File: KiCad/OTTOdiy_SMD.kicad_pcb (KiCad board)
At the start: 4 copper layers, 297 x 170.8 mm, 468 parts, among them CN201 1x4 MALE 1.5mm, CN202 1x4 MALE 1.5mm, J201 RASPBERRY PI 3 A+, J202 Conn_02x03, J203 Conn_02x05, J204 Conn_02x05, J205 Conn_02x04, J206 Conn_02x06, J207 Conn_02x03, Q201 IRF9321PbF, SW1 ALPS SKHC, SW10 ALPS SKHC, SW11 ALPS SKHC, SW12 ALPS SKHC, SW13 ALPS SKHC, SW14 ALPS SKHC, SW15 ALPS SKHC, SW16 ALPS SKHC, SW17 ALPS SKHC, SW18 ALPS SKHC, SW19 ALPS SKHC, SW2 ALPS SKHC, SW20 ALPS SKHC, SW201 SW_Push, SW202 SW_DIP_x02, SW203 ALPS SKHH angled, SW21 ALPS SKHC, SW22 ALPS SKHC, SW23 ALPS SKHC, SW24 ALPS SKHC, SW25 ALPS SKHC, SW26 ALPS SKHC, SW27 6x6x13mm, SW28 6x6x13mm, SW29 6x6x13mm, SW3 ALPS SKHC, SW30 6x6x13mm, SW31 6x6x13mm, SW32 6x6x13mm, SW33 6x6x13mm, SW34 6x6x13mm, SW35 6x6x13mm, SW36 6x6x13mm, SW37 6x6x13mm, SW38 6x6x13mm, SW39 6x6x13mm, SW4 ALPS SKHC, SW40 6x6x13mm, SW41 6x6x13mm, SW42 6x6x13mm, SW43 6x6x13mm, SW44 6x6x13mm, SW45 6x6x13mm, SW46 6x6x13mm, SW47 6x6x13mm, SW5 ALPS SKHC, SW6 ALPS SKHC, SW7 ALPS SKHC, SW8 ALPS SKHC, SW9 ALPS SKHC, U201 TPS79533, U202 STM32F407VGTx, U203 74HC125D, U204 USB6B1, U205 74HC14, U206 H11L1, U207 WM8731-Audio, U208 TPS79533, Y201 8MHz, Y202 32.768kHz, Y203 12.288MHz

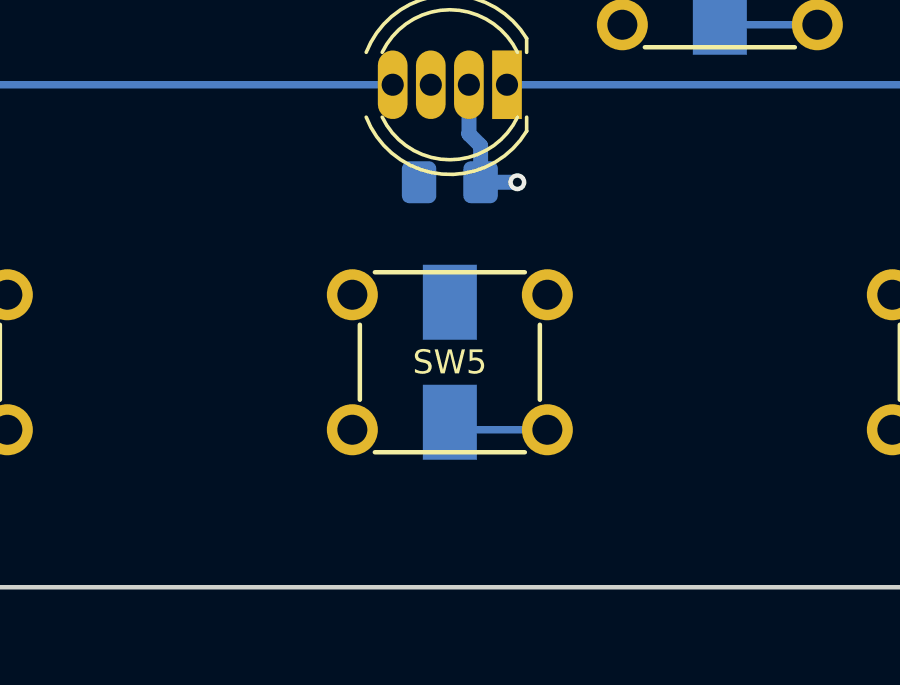
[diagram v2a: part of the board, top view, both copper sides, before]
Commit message: add switch and encoder parts. BM Complete. Footprints complete.
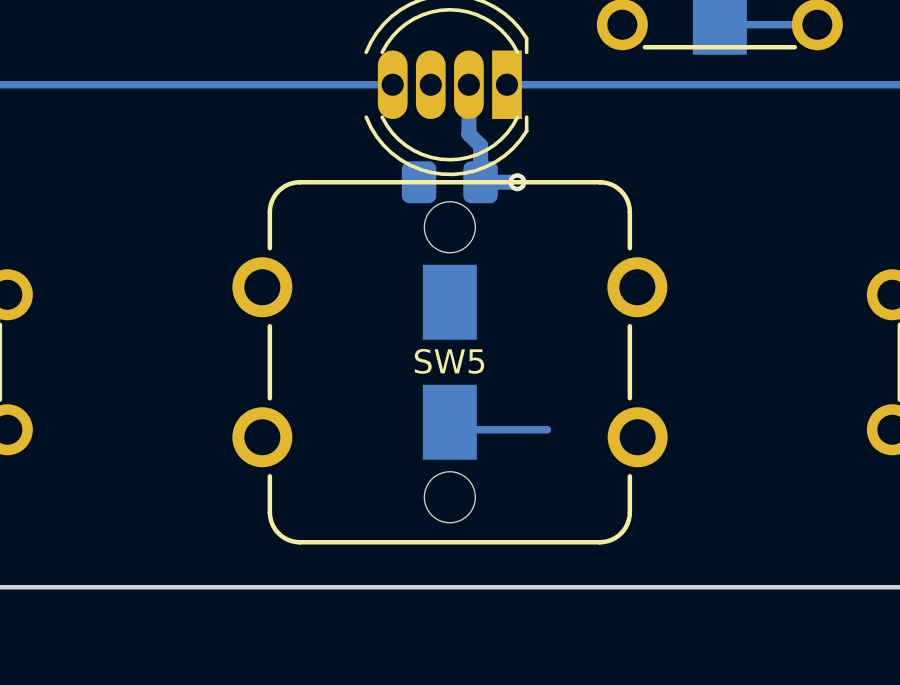
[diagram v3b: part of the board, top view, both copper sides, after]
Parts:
- SW5: footprint Spatz:6x6mm_Switch_LargeCap -> OTTO_Footprints_Lib:ALPS_SKHC

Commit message: Add power switch and other misc nice to haves
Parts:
- removed C201, C208, C209: 10µF, Capacitor_SMD:C_0805_2012Metric_Pad1.15x1.40mm_HandSolder
- removed C202: 1nF/2kV, Capacitor_SMD:C_1206_3216Metric_Pad1.42x1.75mm_HandSolder
- removed C206, C207: 12.5pF, Capacitor_SMD:C_0805_2012Metric_Pad1.15x1.40mm_HandSolder
- removed C228, C229: 1000µF, Capacitor_THT:CP_Radial_D8.0mm_P3.50mm
- removed D201: 5.6V, Diode_SMD:D_SMA
- removed DUMMY201: RASPBERRY PI 3 A+, Spatz:Raspberry Pi A
- removed DUMMY202: FE-PI AUDIO Z V2, Spatz:Raspberry Pi Zero - (minus 1 hole)
- removed F201: 3A, Fuse:Fuse_1806_4516Metric_Pad1.57x1.80mm_HandSolder
- removed the H205 at (306.2, 89.8)
- removed the H205 at (306.2, 31.8)
- removed JP201: SolderJumper_3_Open, Jumper:SolderJumper-3_P2.0mm_Open_TrianglePad1.0x1.5mm
- removed Q201: IRF9321PbF, Package_SO:SOIC-8_3.9x4.9mm_P1.27mm
- removed R201: 1M, Resistor_SMD:R_1206_3216Metric_Pad1.42x1.75mm_HandSolder
- removed R209: 10k, Resistor_SMD:R_0805_2012Metric_Pad1.15x1.40mm_HandSolder
- removed R210: 100k, Resistor_SMD:R_0805_2012Metric_Pad1.15x1.40mm_HandSolder
- removed REF**: PinSocket_2x20_P2.54mm_Vertical_SMD, Connector_PinSocket_2.54mm:PinSocket_2x20_P2.54mm_Vertical_SMD
- removed REF** (x25): SOD-123, digikey-footprints:SOD-123
- removed REF** (x25): LED_WS2812B_PLCC4_5.0x5.0mm_P3.2mm, LED_SMD:LED_WS2812B_PLCC4_5.0x5.0mm_P3.2mm
- removed REF** (x25): SW_SPST_B3S-1000, Button_Switch_SMD:SW_SPST_B3S-1000
- removed REF** (x25): C_0805_2012Metric, Capacitor_SMD:C_0805_2012Metric
- removed REF** (x5): PJ-393-7A, Connector_Audio:PJ-393-7A
- removed REF**: Display_2.8inch_IPS3P4416-H-E, OTTOdiy - SMD - Production:Display_2.8inch_IPS3P4416-H-E
- removed REF** (x4): ALPS_EC12D, Rotary_Encoder:ALPS_EC12D
- removed U201: TPS79533, Package_TO_SOT_SMD:SOT-223-6
- removed U203: 74HC125D, Package_SO:SOIC-14_3.9x8.7mm_P1.27mm
- added C77: 10nF, Capacitor_SMD:C_0805_2012Metric_Pad1.15x1.40mm_HandSolder, F.Cu at (206.8, 54.0)
- added C78: 100nF, Capacitor_SMD:C_0805_2012Metric_Pad1.15x1.40mm_HandSolder, F.Cu at (221.9, 56.9)
- added C79: 470uF, Capacitor_SMD:C_Elec_6.3x7.7, F.Cu at (181.6, 44.6)
- added C80: 10uF, Capacitor_SMD:C_0805_2012Metric_Pad1.15x1.40mm_HandSolder, F.Cu at (198.4, 59.9)
- added C81: 470uF, Capacitor_SMD:C_Elec_6.3x7.7, F.Cu at (192.1, 39.2)
- added C82: 100nF, Capacitor_SMD:C_0805_2012Metric_Pad1.15x1.40mm_HandSolder, F.Cu at (193.6, 63.2)
- added C83: 100nF, Capacitor_SMD:C_0805_2012Metric_Pad1.15x1.40mm_HandSolder, F.Cu at (202.1, 54.0)
- added C84: 470uF, Capacitor_SMD:C_Elec_6.3x7.7, F.Cu at (168.6, 54.9)
- added C85: 1uF, Capacitor_SMD:C_0805_2012Metric_Pad1.15x1.40mm_HandSolder, F.Cu at (203.1, 59.9)
- added C86: 4.7uF, Capacitor_SMD:C_0805_2012Metric_Pad1.15x1.40mm_HandSolder, F.Cu at (203.1, 57.0)
- added C87: 10nF, Capacitor_SMD:C_0805_2012Metric_Pad1.15x1.40mm_HandSolder, F.Cu at (212.7, 45.5)
- added C88: 10uF, Capacitor_SMD:C_0805_2012Metric_Pad1.15x1.40mm_HandSolder, F.Cu at (211.7, 48.4)
- added C89: 22pF, Capacitor_SMD:C_0805_2012Metric_Pad1.15x1.40mm_HandSolder, F.Cu at (198.4, 62.9)
- added C90: 100nF, Capacitor_SMD:C_0805_2012Metric_Pad1.15x1.40mm_HandSolder, F.Cu at (207.0, 50.4)
- added C91: 100nF, Capacitor_SMD:C_0805_2012Metric_Pad1.15x1.40mm_HandSolder, F.Cu at (212.7, 42.5)
- added C92: 680pF, Capacitor_SMD:C_0805_2012Metric_Pad1.15x1.40mm_HandSolder, F.Cu at (202.2, 51.1)
- added C93: 15pF, Capacitor_SMD:C_0805_2012Metric_Pad1.15x1.40mm_HandSolder, F.Cu at (193.6, 60.2)
- added C94: 47pF, Capacitor_SMD:C_0805_2012Metric_Pad1.15x1.40mm_HandSolder, F.Cu at (193.6, 57.3)
- added C95: 47uF, Capacitor_SMD:C_1206_3216Metric_Pad1.42x1.75mm_HandSolder, F.Cu at (172.5, 61.2)
- added C96: 15pF, Capacitor_SMD:C_0805_2012Metric_Pad1.15x1.40mm_HandSolder, F.Cu at (173.5, 72.3)
- added C97: 15pF, Capacitor_SMD:C_0805_2012Metric_Pad1.15x1.40mm_HandSolder, F.Cu at (170.7, 78.1)
- added D48: 15V BI TVS, Diode_SMD:D_SOD-123F, F.Cu at (178.3, 61.2)
- added D49: 15V ZENER, Diode_SMD:D_SOD-123, F.Cu at (198.0, 45.0)
- added D50: 6V BI TVS, Package_TO_SOT_SMD:SOT-323_SC-70_Handsoldering, F.Cu at (192.9, 69.7)
- added D51: 6V BI TVS, Package_TO_SOT_SMD:SOT-323_SC-70_Handsoldering, F.Cu at (192.9, 73.4)
- added D52: 6V BI TVS, Package_TO_SOT_SMD:SOT-323_SC-70_Handsoldering, F.Cu at (198.8, 69.7)
- added D53: 6V BI TVS, Package_TO_SOT_SMD:SOT-323_SC-70_Handsoldering, F.Cu at (192.9, 77.0)
- added D54: 6V BI TVS, Package_TO_SOT_SMD:SOT-323_SC-70_Handsoldering, F.Cu at (198.8, 73.4)
- added D55: 6V BI TVS, Package_TO_SOT_SMD:SOT-323_SC-70_Handsoldering, F.Cu at (204.6, 69.7)
- added D56: 6V BI TVS, Package_TO_SOT_SMD:SOT-323_SC-70_Handsoldering, F.Cu at (198.8, 77.0)
- added FB1: 1kΩ@100Mhz, Inductor_SMD:L_0805_2012Metric_Pad1.15x1.40mm_HandSolder, F.Cu at (175.5, 75.3)
- added J1: Conn_ARM_JTAG_SWD_10, OTTO_Footprints_Lib:FTSH-105-01-X-DV-K, F.Cu at (167.3, 72.3)
- added J2: JST 2-pin SH, Connector_JST:JST_SH_SM02B-SRSS-TB_1x02-1MP_P1.00mm_Horizontal, F.Cu at (115.8, 54.6)
- added J3: JST 2-pin SH, Connector_JST:JST_SH_SM02B-SRSS-TB_1x02-1MP_P1.00mm_Horizontal, F.Cu at (122.7, 54.6)
- added L1: 4.7uH, OTTO_Footprints_Lib:L_7.3x6.6_H3, F.Cu at (201.3, 39.1)
- added L2: 2.2uH, OTTO_Footprints_Lib:L_7.3x6.6_H3, F.Cu at (190.8, 47.2)
- added Q1: AO4485, Package_SO:SOIC-8_3.9x4.9mm_P1.27mm, F.Cu at (185.9, 54.4)
- added R1: 1k, Resistor_SMD:R_0805_2012Metric_Pad1.15x1.40mm_HandSolder, F.Cu at (226.6, 36.6)
- added R10: 100k, Resistor_SMD:R_0805_2012Metric_Pad1.15x1.40mm_HandSolder, F.Cu at (198.4, 57.0)
- added R11: 100k, Resistor_SMD:R_0805_2012Metric_Pad1.15x1.40mm_HandSolder, F.Cu at (227.7, 52.2)
- added R12: 0, Resistor_SMD:R_0805_2012Metric_Pad1.15x1.40mm_HandSolder, F.Cu at (207.0, 47.4)
- added R13: 100k, Resistor_SMD:R_0805_2012Metric_Pad1.15x1.40mm_HandSolder, F.Cu at (188.9, 62.0)
- added R14: 100k, Resistor_SMD:R_0805_2012Metric_Pad1.15x1.40mm_HandSolder, F.Cu at (208.0, 44.2)
- added R15: 100k, Resistor_SMD:R_0805_2012Metric_Pad1.15x1.40mm_HandSolder, F.Cu at (197.5, 48.1)
- added R16: 100k, Resistor_SMD:R_0805_2012Metric_Pad1.15x1.40mm_HandSolder, F.Cu at (203.2, 44.5)
- added R17: 0, Resistor_SMD:R_0805_2012Metric_Pad1.15x1.40mm_HandSolder, F.Cu at (188.9, 59.1)
- added R18: 182k, Resistor_SMD:R_0805_2012Metric_Pad1.15x1.40mm_HandSolder, F.Cu at (208.0, 41.3)
- added R19: 40.2k, Resistor_SMD:R_0805_2012Metric_Pad1.15x1.40mm_HandSolder, F.Cu at (197.5, 51.1)
- added R2: 1k, Resistor_SMD:R_0805_2012Metric_Pad1.15x1.40mm_HandSolder, F.Cu at (221.9, 36.6)
- added R20: 42.2k, Resistor_SMD:R_0805_2012Metric_Pad1.15x1.40mm_HandSolder, F.Cu at (212.8, 36.6)
- added R21: 33k, Resistor_SMD:R_0805_2012Metric_Pad1.15x1.40mm_HandSolder, F.Cu at (202.2, 48.1)
- added R22: 845k, Resistor_SMD:R_0805_2012Metric_Pad1.15x1.40mm_HandSolder, F.Cu at (211.7, 51.4)
- added R23: 158k, Resistor_SMD:R_0805_2012Metric_Pad1.15x1.40mm_HandSolder, F.Cu at (212.8, 39.6)
- added R235: 33, Resistor_SMD:R_0805_2012Metric_Pad1.15x1.40mm_HandSolder, F.Cu at (208.8, 73.0)
- added R236: 33, Resistor_SMD:R_0805_2012Metric_Pad1.15x1.40mm_HandSolder, F.Cu at (204.1, 76.0)
- added R237: 33, Resistor_SMD:R_0805_2012Metric_Pad1.15x1.40mm_HandSolder, F.Cu at (209.9, 69.4)
- added R238: 33, Resistor_SMD:R_0805_2012Metric_Pad1.15x1.40mm_HandSolder, F.Cu at (204.1, 73.0)
- added R24: 10k, Resistor_SMD:R_0805_2012Metric_Pad1.15x1.40mm_HandSolder, F.Cu at (197.3, 54.0)
- added R3: 1k, Resistor_SMD:R_0805_2012Metric_Pad1.15x1.40mm_HandSolder, F.Cu at (221.9, 39.6)
- added R4: 10k, Resistor_SMD:R_0805_2012Metric_Pad1.15x1.40mm_HandSolder, F.Cu at (183.0, 72.3)
- added R5: 10k, Resistor_SMD:R_0805_2012Metric_Pad1.15x1.40mm_HandSolder, F.Cu at (183.0, 69.4)
- added R6: 10k, Resistor_SMD:R_0805_2012Metric_Pad1.15x1.40mm_HandSolder, F.Cu at (178.2, 72.3)
- added R7: 10k, Resistor_SMD:R_0805_2012Metric_Pad1.15x1.40mm_HandSolder, F.Cu at (178.2, 69.4)
- added R8: 40.2k, Resistor_SMD:R_0805_2012Metric_Pad1.15x1.40mm_HandSolder, F.Cu at (173.5, 69.4)
- added R9: 100k, Resistor_SMD:R_0805_2012Metric_Pad1.15x1.40mm_HandSolder, F.Cu at (226.6, 56.9)
- added SW48: SW_DIP_x02, OTTO_Footprints_Lib:SW_DIP_SPSTx02_Slide_HRO_EP-02KS, F.Cu at (181.9, 37.8)
- added SW49: SW_SPDT, Button_Switch_SMD:SW_SPDT_CK-JS102011SAQN, F.Cu at (79.0, 107.7)
- added TP1: TestPoint, TestPoint:TestPoint_Keystone_5000-5004_Miniature, F.Cu at (232.2, 52.9)
- added TP10: TestPoint, TestPoint:TestPoint_Keystone_5000-5004_Miniature, F.Cu at (180.0, 76.0)
- added TP11: TestPoint, TestPoint:TestPoint_Keystone_5000-5004_Miniature, F.Cu at (114.6, 60.6)
- added TP12: TestPoint, TestPoint:TestPoint_Keystone_5000-5004_Miniature, F.Cu at (118.9, 60.6)
- added TP13: TestPoint, TestPoint:TestPoint_Keystone_5000-5004_Miniature, F.Cu at (128.3, 53.0)
- added TP14: TestPoint, TestPoint:TestPoint_Keystone_5000-5004_Miniature, F.Cu at (123.3, 60.6)
- added TP15: TestPoint, TestPoint:TestPoint_Keystone_5000-5004_Miniature, F.Cu at (128.3, 57.3)
- added TP2: TestPoint, TestPoint:TestPoint_Keystone_5000-5004_Miniature, F.Cu at (239.5, 41.7)
- added TP3: TestPoint, TestPoint:TestPoint_Keystone_5000-5004_Miniature, F.Cu at (235.1, 41.7)
- added TP4: TestPoint, TestPoint:TestPoint_Keystone_5000-5004_Miniature, F.Cu at (235.5, 37.3)
- added TP5: TestPoint, TestPoint:TestPoint_Keystone_5000-5004_Miniature, F.Cu at (230.8, 41.7)
- added TP6: TestPoint, TestPoint:TestPoint_Keystone_5000-5004_Miniature, F.Cu at (226.0, 44.6)
- added TP7: TestPoint, TestPoint:TestPoint_Keystone_5000-5004_Miniature, F.Cu at (231.2, 37.3)
- added TP8: TestPoint, TestPoint:TestPoint_Keystone_5000-5004_Miniature, F.Cu at (226.4, 40.3)
- added TP9: TestPoint, TestPoint:TestPoint_Keystone_5000-5004_Miniature, F.Cu at (221.7, 43.2)
- added U1: SN74LV1T125_SOT-23_A, Package_TO_SOT_SMD:SOT-23-5_HandSoldering, F.Cu at (222.4, 53.1)
- added U2: TPS22918_SOT23-6_A, Package_TO_SOT_SMD:SOT-23-6, F.Cu at (208.0, 37.5)
- added U3: LTC3112_TSSOP20_A, OTTO_Footprints_Lib:TSSOP-20_FE_CA, F.Cu at (177.6, 55.6)
- added U4: TLV62568_SOT-23-5_A, Package_TO_SOT_SMD:SOT-23-5, F.Cu at (192.5, 53.5)
- added U5: TPS22918_SOT23-6_A, Package_TO_SOT_SMD:SOT-23-6, F.Cu at (184.1, 59.9)
- BT201: value CR1220 -> CR1220 HOLDER; footprint Battery:QJ1220-2SMT -> OTTO_Footprints_Lib:QJ1220-2SMT
- C1, C10, C11, C12, C13, C14, C15, C16, C17, C18, C19, C2, C20, C21, C22, C23, C24, C25, C26, C27, C28, C29, C3, C30, C31, C32, C33, C34, C35, C36, C37, C38, C39, C4, C40, C41, C42, C43, C44, C45, C46, C47, C48, C49, C5, C50, C51, C52, C53, C54, C55, C56, C58, C59, C6, C60, C61, C62, C63, C64, C65, C66, C67, C68, C69, C7, C70, C71, C72, C73, C74, C75, C8, C9: footprint Capacitor_SMD:C_0805_2012Metric_Pad1.15x1.40mm_HandSolder_marked -> Capacitor_SMD:C_0805_2012Metric_Pad1.15x1.40mm_HandSolder
- C204, C205: value 20pF -> 30pF
- C211: value 4.7µF -> 4.7uF
- C218, C219, C223: value 1µF -> 1uF
- C221, C222: value 2.2µF -> 2.2uF
- C226, C232, C260, C261, C267, C268: value 10µF -> 10uF
- C243, C246, C247, C250, C264: value 10µ -> 10uF
- C251, C253, C254, C255, C257: value 1µF (AUDIO) -> 1uF (AUDIO); footprint Capacitor_THT:C_Rect_L7.2mm_W5.0mm_P5.00mm_FKS2_FKP2_MKS2_MKP2 -> OTTO_Footprints_Lib:C_Rect_L7.2mm_W5.0mm_P5.00mm_FKS2_FKP2_MKS2_MKP2
- C252, C256, C259: value 220p (C0G) -> 220pF (C0G)
- C258, C262: value 220µF -> 220uF
- C265, C266: value 20pF -> 30pF; moved to F.Cu
- C57: footprint Capacitor_SMD:C_0805_2012Metric_Pad1.15x1.40mm_HandSolder_marked -> Capacitor_SMD:C_0805_2012Metric_Pad1.15x1.40mm_HandSolder; moved to F.Cu
- C76: value 100nF -> 47uF; footprint Capacitor_SMD:C_0805_2012Metric_Pad1.15x1.40mm_HandSolder_marked -> Capacitor_SMD:C_1206_3216Metric_Pad1.42x1.75mm_HandSolder; moved to F.Cu
- CN201, CN202: value 1x4 MALE 1.5mm -> 1x4 MALE Molex PicoBlade; footprint Connector_Molex:Molex_PicoBlade_53048-0410_1x04_P1.25mm_Horizontal -> Connector_Molex:Molex_PicoBlade_53261-0471_1x04-1MP_P1.25mm_Horizontal
- D1, D10, D11, D12, D13, D14, D15, D16, D17, D18, D19, D2, D20, D202, D203, D204, D205, D21, D22, D23, D24, D25, D26, D27, D28, D29, D3, D30, D31, D32, D33, D34, D35, D36, D37, D38, D39, D4, D40, D41, D42, D43, D44, D45, D46, D47, D5, D6, D7, D8, D9: value M7 -> SM4007PL; footprint Diode_SMD:D_SMA -> Diode_SMD:D_SOD-123F
- D206: value 1N4148 -> 1N4148W; footprint Diode_SMD:D_SMA -> Diode_SMD:D_SOD-123
- DC201: value Barrel_Jack_Switch -> Barrel Jack, 2.0mmID, 6.5mmOD; footprint Spatz:DC Jack -> OTTO_Footprints_Lib:BarrelJack_2.0mmID_6.5mmOD
- DISPLAY201: value 2.8INCH_IPS_SPI -> 2.8 Inch IPS Display, SPI Interface; footprint Spatz:2.8 INCH IPS DISPLAY -> OTTO_Footprints_Lib:2.8_INCH_IPS_DISPLAY
- ENC1, ENC2, ENC3, ENC4: footprint Spatz:ALPS EC11 -> OTTO_Footprints_Lib:ALPS_EC11
- H201, H202, H203, H204, H205, H206, H207, H208, H209, H210, H211: footprint Spatz:Mounting_Hole_M2.5_Loose_Fit -> OTTO_Footprints_Lib:Mounting_Hole_M2.5_Loose_Fit
- J201: value RASPBERRY PI 3 A+ -> Raspberry Pi Connector; footprint Connector_Harwin:Harwin_M20-7812045_2x20_P2.54mm_Vertical_SolderHoles -> OTTO_Footprints_Lib:Raspberry_Pi_A_FacingDown_TH
- J206: footprint Connector_Harwin:Harwin_M20-7810645_2x06_P2.54mm_Vertical_SolderHoles -> OTTO_Footprints_Lib:Harwin_M20-7810645_2x06_P2.54mm_Vertical_SolderHoles
- J207: footprint Connector_Harwin:Harwin_M20-7810345_2x03_P2.54mm_Vertical_SolderHoles -> OTTO_Footprints_Lib:Harwin_M20-7810345_2x03_P2.54mm_Vertical_SolderHoles
- LED1, LED10, LED11, LED12, LED13, LED14, LED15, LED16, LED17, LED18, LED19, LED2, LED20, LED21, LED22, LED23, LED24, LED25, LED26, LED27, LED28, LED29, LED3, LED30, LED31, LED32, LED33, LED34, LED35, LED36, LED37, LED38, LED39, LED4, LED40, LED41, LED42, LED43, LED44, LED45, LED46, LED47, LED5, LED6, LED7, LED8, LED9: value WS2812D-F5 -> WS2812D-5; footprint Spatz:LED_D5.0mm-4 -> OTTO_Footprints_Lib:LED_D5.0mm-4
- MK201: footprint Sensor_Audio:INGHAi GMI6050p -> OTTO_Footprints_Lib:INGHAi_GMI6050p
- PHOTO201: footprint OptoDevice:ALS-PDIC243-3B -> OTTO_Footprints_Lib:ALS-PDIC243-3B
- R202, R205, R206, R207: value 2k2 -> 2.2k
- R208: value 470 -> 100
- SW1, SW10, SW11, SW12, SW13, SW14, SW15, SW16, SW17, SW18, SW19, SW2, SW20, SW21, SW22, SW23, SW24, SW25, SW26, SW3, SW4, SW6, SW7, SW8, SW9: value ALPS SKHC -> ALPS SKHH OR SKPF; footprint Spatz:6x6mm_Switch_LargeCap -> OTTO_Footprints_Lib:6x6mm_Switch_LargeCap_ALT_SKPF
- SW201: value SW_Push -> 6x6x5mm
- SW202: footprint Button_Switch_THT:XKB_DSIC02LH-P -> OTTO_Footprints_Lib:SW_DIP_SPSTx02_Slide_HRO_EP-02KS
- SW203: value ALPS SKHH angled -> 6x6x5.85mm (RA)
- SW27, SW28, SW29, SW30, SW31, SW32, SW33, SW34, SW35, SW36, SW37, SW38, SW39, SW40, SW41, SW42, SW43, SW44, SW45, SW46, SW47: footprint Spatz:6x6mm_Switch -> OTTO_Footprints_Lib:6x6mm_Switch
- SW5: value ALPS SKHC -> ALPS SKHH OR SKPF; footprint OTTO_Footprints_Lib:ALPS_SKHC -> OTTO_Footprints_Lib:6x6mm_Switch_LargeCap_ALT_SKPF
- TRS201, TRS202, TRS203: value PJ-393-7A -> PJ-3930-8A; footprint Spatz:3.5mm_jack_PJ-3930-8A -> OTTO_Footprints_Lib:3.5mm_jack_PJ-3930-8A
- TRS204, TRS205, TRS206: footprint Spatz:3.5mm_jack_PJ-3930-8A -> OTTO_Footprints_Lib:3.5mm_jack_PJ-3930-8A
- U205: value 74HC14 -> SN74HC14
- U206: value H11L1 -> H11L1S; footprint Package_DIP:DIP-6_W7.62mm_SMDSocket_SmallPads -> Package_DIP:SMDIP-6_W7.62mm
- U207: value WM8731-Audio -> WM8731
- USB201: footprint Spatz:USB_B -> OTTO_Footprints_Lib:USB_B
- Y201, Y203: footprint Crystal:Crystal_HC49-U_Vertical -> Crystal:Crystal_SMD_HC49-SD_HandSoldering
- Y202: footprint Crystal:Crystal_DS26_D2.0mm_L6.0mm_Horizontal -> Crystal:Crystal_SMD_SeikoEpson_MC306-4Pin_8.0x3.2mm_HandSoldering
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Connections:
- net +5V_IN renamed +5V_REG
- net /AUDIO/XTI renamed Net-(C265-Pad1)
- net /AUDIO/XTO renamed Net-(C266-Pad1)
- C1 pad 1: +5V_MAIN -> +5V_LEDS
- C10 pad 1: +5V_MAIN -> +5V_LEDS
- C11 pad 1: +5V_MAIN -> +5V_LEDS
- C12 pad 1: +5V_MAIN -> +5V_LEDS
- C13 pad 1: +5V_MAIN -> +5V_LEDS
- C14 pad 1: +5V_MAIN -> +5V_LEDS
- C15 pad 1: +5V_MAIN -> +5V_LEDS
- C16 pad 1: +5V_MAIN -> +5V_LEDS
- C17 pad 1: +5V_MAIN -> +5V_LEDS
- C18 pad 1: +5V_MAIN -> +5V_LEDS
- C19 pad 1: +5V_MAIN -> +5V_LEDS
- C2 pad 1: +5V_MAIN -> +5V_LEDS
- C20 pad 1: +5V_MAIN -> +5V_LEDS
- C21 pad 1: +5V_MAIN -> +5V_LEDS
- C219 pad 1: +3V3_MCU -> +3V3A_MCU
- C22 pad 1: +5V_MAIN -> +5V_LEDS
- C223 pad 1: Net-(C223-Pad1) -> +3V3A_MCU
- C23 pad 1: +5V_MAIN -> +5V_LEDS
- C24 pad 1: +5V_MAIN -> +5V_LEDS
- C25 pad 1: +5V_MAIN -> +5V_LEDS
- C26 pad 1: +5V_MAIN -> +5V_LEDS
- C261 pad 2: +5V_MAIN -> +5V_PI
- C267 pad 2: +5V_MAIN -> +5V_PI
- C27 pad 1: +5V_MAIN -> +5V_LEDS
- C28 pad 1: +5V_MAIN -> +5V_LEDS
- C29 pad 1: +5V_MAIN -> +5V_LEDS
- C3 pad 1: +5V_MAIN -> +5V_LEDS
- C30 pad 1: +5V_MAIN -> +5V_LEDS
- C31 pad 1: +5V_MAIN -> +5V_LEDS
- C32 pad 1: +5V_MAIN -> +5V_LEDS
- C33 pad 1: +5V_MAIN -> +5V_LEDS
- C34 pad 1: +5V_MAIN -> +5V_LEDS
- C35 pad 1: +5V_MAIN -> +5V_LEDS
- C36 pad 1: +5V_MAIN -> +5V_LEDS
- C37 pad 1: +5V_MAIN -> +5V_LEDS
- C38 pad 1: +5V_MAIN -> +5V_LEDS
- C39 pad 1: +5V_MAIN -> +5V_LEDS
- C4 pad 1: +5V_MAIN -> +5V_LEDS
- C40 pad 1: +5V_MAIN -> +5V_LEDS
- C41 pad 1: +5V_MAIN -> +5V_LEDS
- C42 pad 1: +5V_MAIN -> +5V_LEDS
- C43 pad 1: +5V_MAIN -> +5V_LEDS
- C44 pad 1: +5V_MAIN -> +5V_LEDS
- C45 pad 1: +5V_MAIN -> +5V_LEDS
- C46 pad 1: +5V_MAIN -> +5V_LEDS
- C47 pad 1: +5V_MAIN -> +5V_LEDS
- C48 pad 2: ICP_RST -> /ICP_RST
- C5 pad 1: +5V_MAIN -> +5V_LEDS
- C55 pad 1: +3V3_MCU -> +3V3A_MCU
- C56 pad 1: Net-(C223-Pad1) -> +3V3A_MCU
- C57 pad 1: +5V_MCU -> GND
- C57 pad 2: GND -> Net-(C57-Pad2)
- C6 pad 1: +5V_MAIN -> +5V_LEDS
- C7 pad 1: +5V_MAIN -> +5V_LEDS
- C76 pad 1: Net-(C76-Pad1) -> /MCU/PERIPHERALS/+5V_REG
- C8 pad 1: +5V_MAIN -> +5V_LEDS
- C9 pad 1: +5V_MAIN -> +5V_LEDS
- CN201 pad 1: Net-(CN201-Pad1) -> (no net)
- CN202 pad 3: Net-(CN202-Pad3) -> (no net)
- D1 pad 1: Net-(D1-Pad1) -> /MCU/ROW_4
- D10 pad 1: Net-(D10-Pad1) -> /MCU/ROW_6
- D11 pad 1: Net-(D11-Pad1) -> /MCU/ROW_8
- D12 pad 1: Net-(D12-Pad1) -> /MCU/ROW_2
- D13 pad 1: Net-(D13-Pad1) -> /MCU/ROW_3
- D14 pad 1: Net-(D14-Pad1) -> /MCU/ROW_5
- D15 pad 1: Net-(D15-Pad1) -> /MCU/ROW_6
- D16 pad 1: Net-(D16-Pad1) -> /MCU/ROW_5
- D17 pad 1: Net-(D17-Pad1) -> /MCU/ROW_1
- D18 pad 1: Net-(D18-Pad1) -> /MCU/ROW_4
- D19 pad 1: Net-(D19-Pad1) -> /MCU/ROW_7
- D2 pad 1: Net-(D2-Pad1) -> /MCU/ROW_2
- D20 pad 1: Net-(D20-Pad1) -> /MCU/ROW_1
- D202 pad 1: Net-(D202-Pad1) -> /MCU/ROW_1
- D203 pad 1: Net-(D203-Pad1) -> /MCU/ROW_2
- D204 pad 1: Net-(D204-Pad1) -> /MCU/ROW_7
- D205 pad 1: Net-(D205-Pad1) -> /MCU/ROW_4
- D21 pad 1: Net-(D21-Pad1) -> /MCU/ROW_4
- D22 pad 1: Net-(D22-Pad1) -> /MCU/ROW_7
- D23 pad 1: Net-(D23-Pad1) -> /MCU/ROW_8
- D24 pad 1: Net-(D24-Pad1) -> /MCU/ROW_1
- D25 pad 1: Net-(D25-Pad1) -> /MCU/ROW_4
- D26 pad 1: Net-(D26-Pad1) -> /MCU/ROW_7
- D27 pad 1: Net-(D27-Pad1) -> /MCU/ROW_3
- D28 pad 1: Net-(D28-Pad1) -> /MCU/ROW_2
- D29 pad 1: Net-(D29-Pad1) -> /MCU/ROW_4
- D3 pad 1: Net-(D3-Pad1) -> /MCU/ROW_3
- D30 pad 1: Net-(D30-Pad1) -> /MCU/ROW_3
- D31 pad 1: Net-(D31-Pad1) -> /MCU/ROW_5
- D32 pad 1: Net-(D32-Pad1) -> /MCU/ROW_6
- D33 pad 1: Net-(D33-Pad1) -> /MCU/ROW_6
- D34 pad 1: Net-(D34-Pad1) -> /MCU/ROW_2
- D35 pad 1: Net-(D35-Pad1) -> /MCU/ROW_2
- D36 pad 1: Net-(D36-Pad1) -> /MCU/ROW_3
- D37 pad 1: Net-(D37-Pad1) -> /MCU/ROW_5
- D38 pad 1: Net-(D38-Pad1) -> /MCU/ROW_7
- D39 pad 1: Net-(D39-Pad1) -> /MCU/ROW_7
- D4 pad 1: Net-(D4-Pad1) -> /MCU/ROW_5
- D40 pad 1: Net-(D40-Pad1) -> /MCU/ROW_7
- D41 pad 1: Net-(D41-Pad1) -> /MCU/ROW_1
- D42 pad 1: Net-(D42-Pad1) -> /MCU/ROW_1
- D43 pad 1: Net-(D43-Pad1) -> /MCU/ROW_4
- D44 pad 1: Net-(D44-Pad1) -> /MCU/ROW_6
- D45 pad 1: Net-(D45-Pad1) -> /MCU/ROW_8
- D46 pad 1: Net-(D46-Pad1) -> /MCU/ROW_8
- D47 pad 1: Net-(D47-Pad1) -> /MCU/ROW_8
- D5 pad 1: Net-(D5-Pad1) -> /MCU/ROW_6
- D6 pad 1: Net-(D6-Pad1) -> /MCU/ROW_8
- D7 pad 1: Net-(D7-Pad1) -> /MCU/ROW_2
- D8 pad 1: Net-(D8-Pad1) -> /MCU/ROW_3
- D9 pad 1: Net-(D9-Pad1) -> /MCU/ROW_5
- DC201 pad 3: Net-(DC201-Pad3) -> (no net)
- H212 pad 1: Net-(C202-Pad1) -> GND
- J201 pad 18: ICP_SWDIO -> Net-(J201-Pad18)
- J201 pad 2: +5V_MAIN -> +5V_PI
- J201 pad 21: SPI_MISO_RASPI -> /SPI_MISO_RASPI
- J201 pad 22: ICP_SWCLK -> Net-(J201-Pad22)
- J201 pad 29: PWR_BUTTON -> Net-(J201-Pad29)
- J201 pad 31: Net-(J201-Pad31) -> PI_PWR_EN
- J201 pad 32: Net-(J201-Pad32) -> BL_PWM
- J201 pad 33: Net-(J201-Pad33) -> /RPI_PWM1_GPIO13
- J201 pad 4: +5V_MAIN -> +5V_PI
- J201 pad 7: ICP_RST -> Net-(J201-Pad7)
- J202 pad 3: +5V_MCU -> +5V_PI
- J202 pad 4: +5V_MCU -> +5V_PI
- J203 pad 2: ICP_RST -> (no net)
- J203 pad 4: ICP_SWDIO -> MIDI_OUT
- J203 pad 6: ICP_SWCLK -> MIDI_IN
- J206 pad 2: +5V_MAIN -> +5V_PI
- J206 pad 4: +5V_MAIN -> +5V_PI
- LED1 pad 2: +5V_MAIN -> +5V_LEDS
- LED10 pad 2: +5V_MAIN -> +5V_LEDS
- LED11 pad 2: +5V_MAIN -> +5V_LEDS
- LED12 pad 2: +5V_MAIN -> +5V_LEDS
- LED13 pad 2: +5V_MAIN -> +5V_LEDS
- LED14 pad 2: +5V_MAIN -> +5V_LEDS
- LED15 pad 2: +5V_MAIN -> +5V_LEDS
- LED16 pad 2: +5V_MAIN -> +5V_LEDS
- LED17 pad 2: +5V_MAIN -> +5V_LEDS
- LED18 pad 2: +5V_MAIN -> +5V_LEDS
- LED19 pad 2: +5V_MAIN -> +5V_LEDS
- LED2 pad 2: +5V_MAIN -> +5V_LEDS
- LED20 pad 2: +5V_MAIN -> +5V_LEDS
- LED21 pad 2: +5V_MAIN -> +5V_LEDS
- LED22 pad 2: +5V_MAIN -> +5V_LEDS
- LED23 pad 2: +5V_MAIN -> +5V_LEDS
- LED24 pad 2: +5V_MAIN -> +5V_LEDS
- LED25 pad 2: +5V_MAIN -> +5V_LEDS
- LED26 pad 2: +5V_MAIN -> +5V_LEDS
- LED27 pad 2: +5V_MAIN -> +5V_LEDS
- LED28 pad 2: +5V_MAIN -> +5V_LEDS
- LED29 pad 2: +5V_MAIN -> +5V_LEDS
- LED3 pad 2: +5V_MAIN -> +5V_LEDS
- LED30 pad 2: +5V_MAIN -> +5V_LEDS
- LED31 pad 2: +5V_MAIN -> +5V_LEDS
- LED32 pad 2: +5V_MAIN -> +5V_LEDS
- LED33 pad 2: +5V_MAIN -> +5V_LEDS
- LED34 pad 2: +5V_MAIN -> +5V_LEDS
- LED35 pad 2: +5V_MAIN -> +5V_LEDS
- LED36 pad 2: +5V_MAIN -> +5V_LEDS
- LED37 pad 2: +5V_MAIN -> +5V_LEDS
- LED38 pad 2: +5V_MAIN -> +5V_LEDS
- LED39 pad 2: +5V_MAIN -> +5V_LEDS
- LED4 pad 2: +5V_MAIN -> +5V_LEDS
- LED40 pad 2: +5V_MAIN -> +5V_LEDS
- LED41 pad 2: +5V_MAIN -> +5V_LEDS
- LED42 pad 2: +5V_MAIN -> +5V_LEDS
- LED43 pad 2: +5V_MAIN -> +5V_LEDS
- LED44 pad 2: +5V_MAIN -> +5V_LEDS
- LED45 pad 2: +5V_MAIN -> +5V_LEDS
- LED46 pad 2: +5V_MAIN -> +5V_LEDS
- LED47 pad 2: +5V_MAIN -> +5V_LEDS
- LED5 pad 2: +5V_MAIN -> +5V_LEDS
- LED6 pad 2: +5V_MAIN -> +5V_LEDS
- LED7 pad 2: +5V_MAIN -> +5V_LEDS
- LED8 pad 2: +5V_MAIN -> +5V_LEDS
- LED9 pad 2: +5V_MAIN -> +5V_LEDS
- PHOTO201 pad 1: +3V3_MCU -> +3V3A_MCU
- R208 pad 1: Net-(JP201-Pad2) -> /MCU/LEDS/LED_IN
- R208 pad 2: Net-(R208-Pad2) -> /MCU/LEDS/SPI_MOSI_MCU_5V
- R218 pad 2: Net-(R218-Pad2) -> /AUDIO/LINE_IN_L
- SW1 pad 2: Net-(SW1-Pad2) -> /MCU/COL_4
- SW10 pad 2: Net-(SW10-Pad2) -> /MCU/COL_2
- SW11 pad 2: Net-(SW11-Pad2) -> /MCU/COL_3
- SW12 pad 2: Net-(SW12-Pad2) -> /MCU/COL_3
- SW13 pad 2: Net-(SW13-Pad2) -> /MCU/COL_3
- SW14 pad 2: Net-(SW14-Pad2) -> /MCU/COL_3
- SW15 pad 2: Net-(SW15-Pad2) -> /MCU/COL_3
- SW16 pad 2: Net-(SW16-Pad2) -> /MCU/COL_4
- SW17 pad 2: Net-(SW17-Pad2) -> /MCU/COL_1
- SW18 pad 2: Net-(SW18-Pad2) -> /MCU/COL_1
- SW19 pad 2: Net-(SW19-Pad2) -> /MCU/COL_1
- SW2 pad 2: Net-(SW2-Pad2) -> /MCU/COL_1
- SW20 pad 2: Net-(SW20-Pad2) -> /MCU/COL_2
- SW201 pad 1: ICP_RST -> /ICP_RST
- SW21 pad 2: Net-(SW21-Pad2) -> /MCU/COL_2
- SW22 pad 2: Net-(SW22-Pad2) -> /MCU/COL_2
- SW23 pad 2: Net-(SW23-Pad2) -> /MCU/COL_2
- SW24 pad 2: Net-(SW24-Pad2) -> /MCU/COL_3
- SW25 pad 2: Net-(SW25-Pad2) -> /MCU/COL_3
- SW26 pad 2: Net-(SW26-Pad2) -> /MCU/COL_3
- SW27 pad 2: Net-(SW27-Pad2) -> /MCU/COL_4
- SW28 pad 2: Net-(SW28-Pad2) -> /MCU/COL_6
- SW29 pad 2: Net-(SW29-Pad2) -> /MCU/COL_6
- SW3 pad 2: Net-(SW3-Pad2) -> /MCU/COL_1
- SW30 pad 2: Net-(SW30-Pad2) -> /MCU/COL_6
- SW31 pad 2: Net-(SW31-Pad2) -> /MCU/COL_6
- SW32 pad 2: Net-(SW32-Pad2) -> /MCU/COL_6
- SW33 pad 2: Net-(SW33-Pad2) -> /MCU/COL_4
- SW34 pad 2: Net-(SW34-Pad2) -> /MCU/COL_4
- SW35 pad 2: Net-(SW35-Pad2) -> /MCU/COL_5
- SW36 pad 2: Net-(SW36-Pad2) -> /MCU/COL_5
- SW37 pad 2: Net-(SW37-Pad2) -> /MCU/COL_5
- SW38 pad 2: Net-(SW38-Pad2) -> /MCU/COL_5
- SW39 pad 2: Net-(SW39-Pad2) -> /MCU/COL_6
- SW4 pad 2: Net-(SW4-Pad2) -> /MCU/COL_1
- SW40 pad 2: Net-(SW40-Pad2) -> /MCU/COL_4
- SW41 pad 2: Net-(SW41-Pad2) -> /MCU/COL_4
- SW42 pad 2: Net-(SW42-Pad2) -> /MCU/COL_5
- SW43 pad 2: Net-(SW43-Pad2) -> /MCU/COL_5
- SW44 pad 2: Net-(SW44-Pad2) -> /MCU/COL_5
- SW45 pad 2: Net-(SW45-Pad2) -> /MCU/COL_5
- SW46 pad 2: Net-(SW46-Pad2) -> /MCU/COL_6
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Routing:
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- removed copper zone on B.Cu, net +5V_MAIN
- removed copper zone on B.Cu, net +5V_MCU
- removed copper zone on B.Cu, net Net-(D48-Pad1)
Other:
- board size 297 x 170.8 mm -> 297 x 91 mm

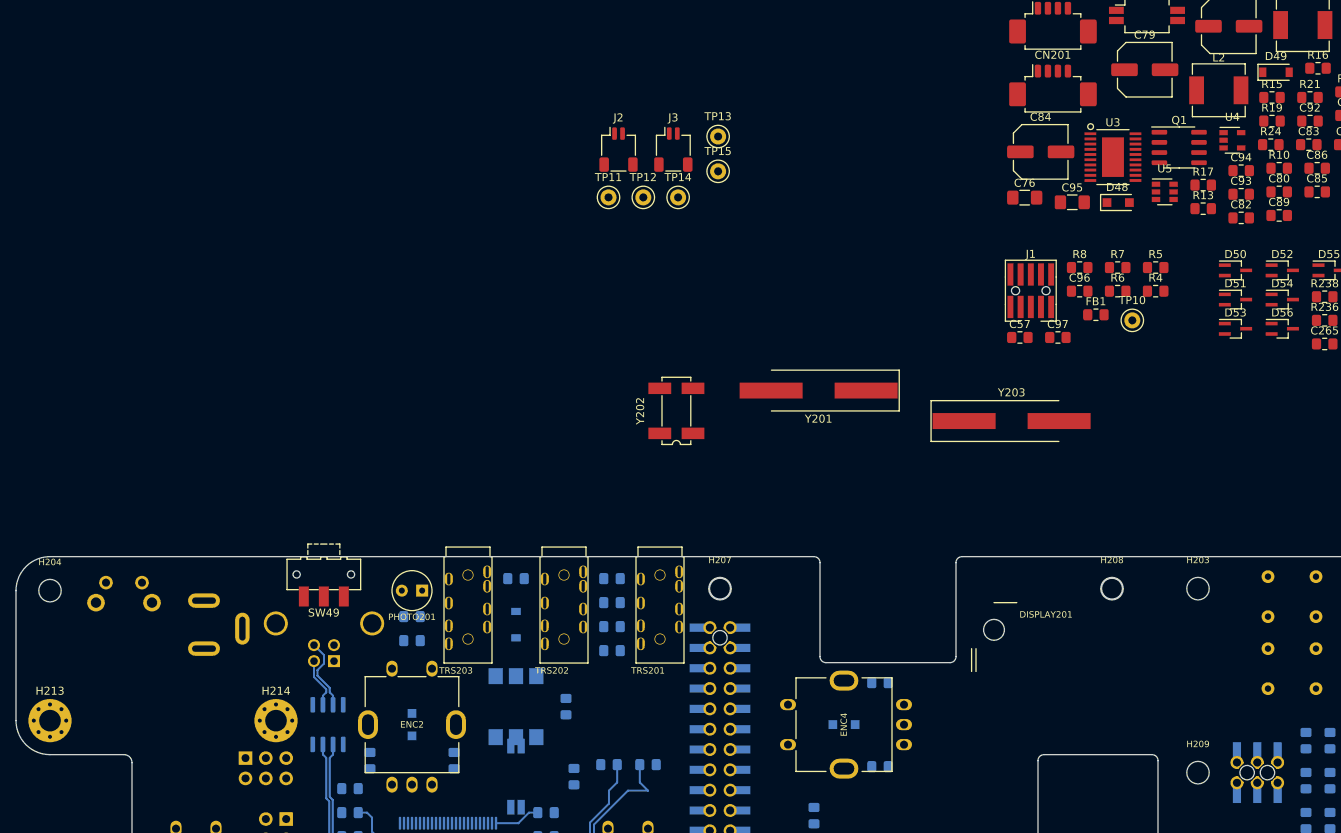
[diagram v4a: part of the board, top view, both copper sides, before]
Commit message: Fixes for external battery board and Routing started
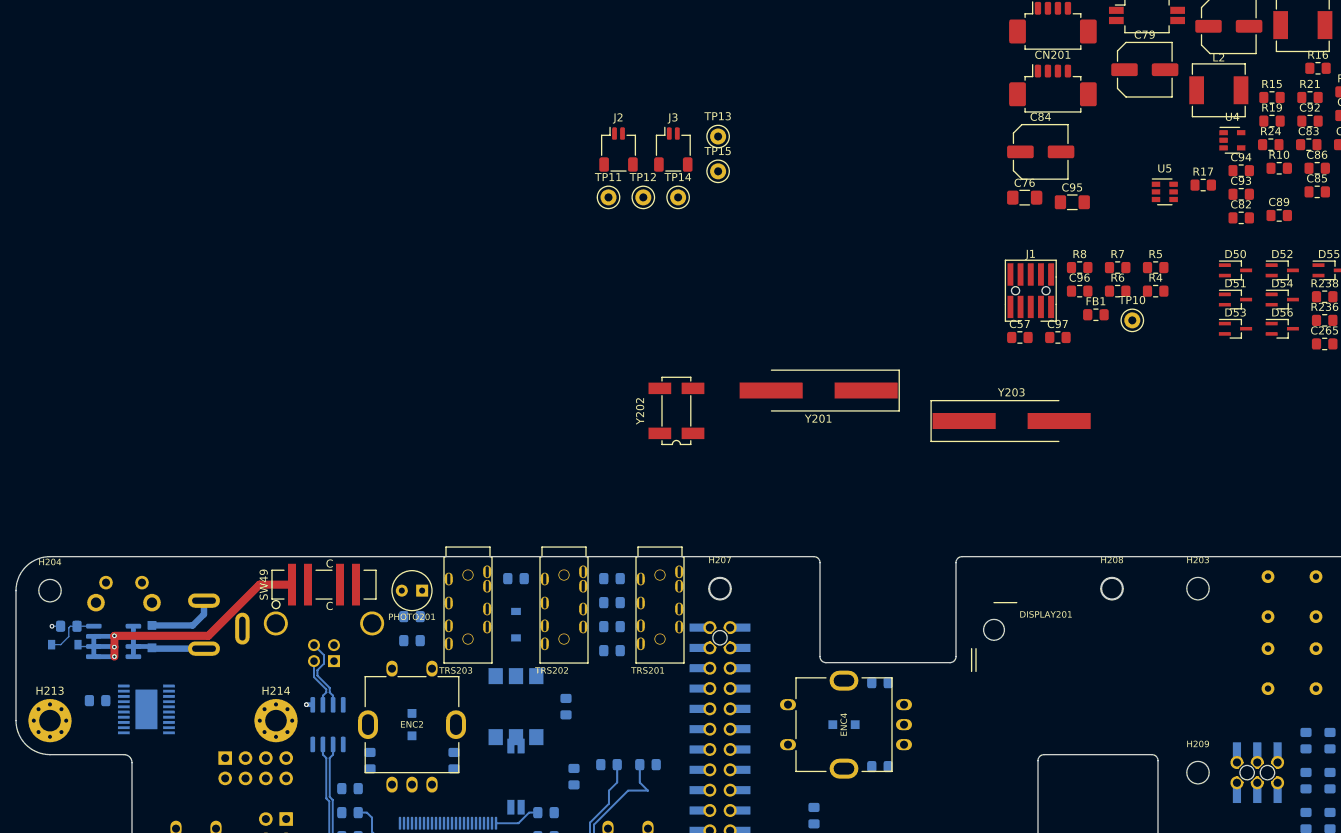
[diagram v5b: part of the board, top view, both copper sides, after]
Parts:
- C80, D48, D49, Q1, R13, U3: moved to B.Cu
- J202: value Conn_02x03 -> Conn_02x04; footprint Connector_PinHeader_2.54mm:PinHeader_2x03_P2.54mm_Vertical -> Connector_PinHeader_2.54mm:PinHeader_2x04_P2.54mm_Vertical
- PHOTO201: value ALS-PDIC243-3B -> VAL**
- SW49: value SW_SPDT -> SW_SP3T (DP3T Parallel); footprint Button_Switch_SMD:SW_SPDT_CK-JS102011SAQN -> OTTO_Footprints_Lib:SW_SP3T_CK-JS203011JCQN
- USB201: value USB_B -> VAL**
- moved D49 167.5 mm to (46.6, 116.5), turned to 180 degrees
- moved C80 160.8 mm to (50.7, 123.5)
- moved R13 151.1 mm to (47.1, 114.2), turned to 180 degrees
- moved Q1 146.8 mm to (52.7, 116.1)
- moved U3 139.2 mm to (56.8, 124.6)
- moved D48 132.4 mm to (57.5, 115.5), turned to 90 degrees
- moved J202 2.54 mm to (66.7, 130.7)
- moved SW49 1.27 mm to (79.0, 109.0), turned to 0 degrees
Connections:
- net /RPI_PWM1_GPIO13 renamed /PWM1_GPIO13_RASPI
- net Net-(J201-Pad11) renamed /GPIO17_RASPI
- net Net-(J201-Pad36) renamed /GPIO16_RASPI
- C261 pad 2: +5V_PI -> +5V_RASPI
- C267 pad 2: +5V_PI -> +5V_RASPI
- C82 pad 1: Net-(C82-Pad1) -> /MCU/5V_RUN
- D49 pad 1: /MCU/PERIPHERALS/BARREL_IN -> /MCU/BARREL_IN
- J201 pad 13: TRIGGER3 -> /GPIO27_RASPI
- J201 pad 16: Net-(J201-Pad16) -> TRIGGER2
- J201 pad 18: Net-(J201-Pad18) -> TRIGGER3
- J201 pad 2: +5V_PI -> +5V_RASPI
- J201 pad 37: TRIGGER2 -> /GPIO26_RASPI
- J201 pad 4: +5V_PI -> +5V_RASPI
- J202 pad 1: +5V_REG -> /MCU/BARREL_IN
- J202 pad 2: +5V_REG -> /MCU/BARREL_IN
- J202 pad 3: +5V_PI -> /MCU/BATT_IN
- J202 pad 4: +5V_PI -> /MCU/BATT_IN
- J202 pad 5: GND -> /MCU/+5V_USB
- J202 pad 6: GND -> /MCU/+5V_USB
- J203 pad 2: (no net) -> /MCU/5V_RUN
- J203 pad 4: MIDI_OUT -> /ICP_SWDIO
- J203 pad 6: MIDI_IN -> /ICP_SWCLK
- J206 pad 2: +5V_PI -> +5V_RASPI
- J206 pad 4: +5V_PI -> +5V_RASPI
- Q1 pad 1: /MCU/PERIPHERALS/BARREL_IN -> /MCU/BARREL_IN
- Q1 pad 2: /MCU/PERIPHERALS/BARREL_IN -> /MCU/BARREL_IN
- Q1 pad 3: /MCU/PERIPHERALS/BARREL_IN -> /MCU/BARREL_IN
- R15 pad 2: Net-(C82-Pad1) -> /MCU/5V_RUN
- R17 pad 1: +5V_PI -> +5V_RASPI
- SW49 pad 1: /MCU/+5V_USB -> /MCU/BARREL_IN
- SW49 pad 2: /MCU/DC_IN -> /MCU/BATT_IN
- SW49 pad 3: /MCU/PERIPHERALS/BARREL_IN -> /MCU/DC_IN
- TP2 pad 1: Net-(J201-Pad16) -> /GPIO26_RASPI
- TP3 pad 1: Net-(J201-Pad18) -> /GPIO27_RASPI
- U208 pad 1: +5V_PI -> +5V_RASPI
- U208 pad 2: +5V_PI -> +5V_RASPI
- U3 pad 7: Net-(C82-Pad1) -> /MCU/5V_RUN
- U5 pad 6: +5V_PI -> +5V_RASPI
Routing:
- net /MCU/BARREL_IN: track 0.00 -> 42.8 mm, vias 0 -> 3
- net Net-(D48-Pad1): track 0.00 -> 12.8 mm
- net GND: track 4.27 -> 14.9 mm, vias 0 -> 2
- net Net-(D49-Pad2): track 0.00 -> 6.87 mm
- net +5V_RASPI: track 0.00 -> 6.24 mm
- net +5V_PI: track 6.24 -> 0.00 mm
- net /MCU/DC_IN: track 0.00 -> 3.00 mm
- net /MCU/BATT_IN: track 0.00 -> 3.00 mm
- net /MCU/+5V_USB: track 0.00 -> 3.00 mm
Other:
- net class Default: via_dia 0.45 -> 0.6; via_drill 0.25 -> 0.3
- net class HIGH POWER removed
- net class LOW POWER removed
- net class MID POWER removed
- rule solder_mask_min_width: 0.25 -> 0.12
- rule trace_min: 0.15 -> 0.127
- rule via_min_drill: 0.2 -> 0.3
- rule via_min_size: 0.45 -> 0.6

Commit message: routed buck boost supply
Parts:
- removed J3: JST 2-pin SH, Connector_JST:JST_SH_SM02B-SRSS-TB_1x02-1MP_P1.00mm_Horizontal
- removed TP1, TP11, TP12, TP13, TP14, TP2, TP3, TP4, TP5: TestPoint, TestPoint:TestPoint_Keystone_5000-5004_Miniature
- added R25: 10k, Resistor_SMD:R_0805_2012Metric_Pad1.15x1.40mm_HandSolder, F.Cu at (112.0, 68.8)
- added R26: 100k, Resistor_SMD:R_0805_2012Metric_Pad1.15x1.40mm_HandSolder, F.Cu at (92.3, 68.8)
- added R27: 100, Resistor_SMD:R_0805_2012Metric_Pad1.15x1.40mm_HandSolder, F.Cu at (112.0, 74.9)
- added TP16: TestPoint, TestPoint:TestPoint_Keystone_5000-5004_Miniature, F.Cu at (76.2, 89.8)
- added TP17: TestPoint, TestPoint:TestPoint_Keystone_5000-5004_Miniature, F.Cu at (80.5, 89.8)
- added TP18: TestPoint, TestPoint:TestPoint_Keystone_5000-5004_Miniature, F.Cu at (84.9, 89.8)
- C258, C262: footprint Capacitor_THT:CP_Radial_D10.0mm_P5.00mm -> Capacitor_THT:CP_Radial_D6.3mm_P2.50mm
- C82, C83, C85, C89, C90, C91, C92, C94, C95, L1, R14, R15, R20, R21, R22, R23, R24: moved to B.Cu
- J2: value JST 2-pin SH -> Conn_02x04; footprint Connector_JST:JST_SH_SM02B-SRSS-TB_1x02-1MP_P1.00mm_Horizontal -> Connector_PinHeader_2.54mm:PinHeader_2x04_P2.54mm_Vertical
- R203, R204, R4, R6, R7: value 10k -> 47k
- moved R23 194.8 mm to (45.5, 139.2), turned to 90 degrees
- moved R14 193.5 mm to (44.6, 147.9), turned to 180 degrees
- moved C91 191.3 mm to (52.3, 146.6), turned to 180 degrees
- moved R22 189.8 mm to (45.5, 142.9), turned to 90 degrees
- moved L1 188.1 mm to (50.3, 151.1), turned to 180 degrees
- moved R20 185.5 mm to (55.5, 134.7), turned to 90 degrees
- moved C85 180.4 mm to (44.6, 146.0), turned to 180 degrees
- moved C83 179.3 mm to (48.6, 146.6), turned to 180 degrees
- moved C92 177.0 mm to (45.3, 132.8), turned to 270 degrees
- moved R21 176.7 mm to (47.2, 132.8), turned to 90 degrees
- moved R24 175.8 mm to (43.6, 139.2), turned to 90 degrees
- moved C94 172.8 mm to (43.6, 142.9), turned to 90 degrees
- moved C90 171.8 mm to (57.4, 134.7), turned to 90 degrees
- moved R15 168.8 mm to (50.2, 130.5), turned to 90 degrees
- moved C89 168.6 mm to (46.3, 135.6)
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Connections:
- net /MCU/PERIPHERALS/USBD__N renamed /MCU/PERIPHERALS/USBD_N_CON
- net /MCU/PERIPHERALS/USBD__P renamed /MCU/PERIPHERALS/USBD_P_CON
- net Net-(C57-Pad2) renamed /MCU/DC_IN_DIV_5
- net Net-(C83-Pad1) renamed /MCU/PERIPHERALS/SW1
- net Net-(C91-Pad1) renamed /MCU/PERIPHERALS/SW2
- C76 pad 1: /MCU/PERIPHERALS/+5V_REG -> +5V_REG
- C79 pad 1: /MCU/PERIPHERALS/+5V_REG -> +5V_REG
- C81 pad 1: /MCU/PERIPHERALS/+5V_REG -> +5V_REG
- C84 pad 1: /MCU/PERIPHERALS/+5V_REG -> +5V_REG
- C86 pad 1: /MCU/PERIPHERALS/+5V_REG -> +5V_REG
- C94 pad 1: /MCU/PERIPHERALS/+5V_REG -> +5V_REG
- C95 pad 1: /MCU/PERIPHERALS/+5V_REG -> +5V_REG
- J2 pad 1: /AUDIO/AMP_OUT_L -> +5V_REG
- J2 pad 2: GND -> HP_SENSE
- J201 pad 11: /GPIO17_RASPI -> AMP_ENABLE
- J201 pad 13: /GPIO27_RASPI -> LO_SENSE
- J201 pad 22: Net-(J201-Pad22) -> HP_SENSE
- J201 pad 27: Net-(J201-Pad27) -> /GPIO0_RASPI
- J201 pad 28: Net-(J201-Pad28) -> /GPIO1_RASPI
- J201 pad 36: /GPIO16_RASPI -> Net-(J201-Pad36)
- J201 pad 37: /GPIO26_RASPI -> LI_SENSE
- R2 pad 2: Net-(J201-Pad22) -> Net-(J201-Pad36)
- R22 pad 1: /MCU/PERIPHERALS/+5V_REG -> +5V_REG
- SW48 pad 1: /MCU/PERIPHERALS/+5V_REG -> +5V_REG
- SW48 pad 2: /MCU/PERIPHERALS/+5V_REG -> +5V_REG
- TP6 pad 1: Net-(J201-Pad27) -> /GPIO0_RASPI
- TP7 pad 1: Net-(J201-Pad28) -> /GPIO1_RASPI
- U2 pad 1: /MCU/PERIPHERALS/+5V_REG -> +5V_REG
- U202 pad 1: (no net) -> (F427)_SAI1_MCLK_A
- U202 pad 55: TRIGGER3 -> (no net)
- U202 pad 56: HP_SENSE -> (no net)
- U202 pad 57: LO_SENSE -> (no net)
- U202 pad 58: LI_SENSE -> (no net)
- U202 pad 59: (no net) -> TRIGGER1
- U202 pad 60: (no net) -> TRIGGER2
- U202 pad 61: (no net) -> TRIGGER3
- U202 pad 63: (no net) -> /GPIO0_RASPI
- U202 pad 64: (no net) -> /GPIO1_RASPI
- U202 pad 65: (no net) -> /PWM1_GPIO13_RASPI
- U202 pad 81: PI_PWR_EN -> Net-(R25-Pad1)
- U202 pad 82: TRIGGER1 -> (no net)
- U202 pad 83: TRIGGER2 -> (no net)
- U202 pad 89: (no net) -> /MCU/SPI_SCLK_MCU
- U202 pad 90: (no net) -> /MCU/SPI_MISO_MCU
- U3 pad 9: /MCU/PERIPHERALS/+5V_REG -> +5V_REG
- U4 pad 1: /MCU/PERIPHERALS/+5V_REG -> +5V_REG
- U4 pad 4: /MCU/PERIPHERALS/+5V_REG -> +5V_REG
- U5 pad 1: /MCU/PERIPHERALS/+5V_REG -> +5V_REG
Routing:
- net /MCU/+5V_USB: track 3.00 -> 36.9 mm
- net GND: track 14.9 -> 42.8 mm, vias 2 -> 16
- net Net-(C89-Pad2): track 0.00 -> 19.1 mm
- net /MCU/5V_RUN: track 0.00 -> 12.4 mm, vias 0 -> 2
- net /MCU/BARREL_IN: track 42.8 -> 33.8 mm
- net /MCU/5V_REG_IOUT: track 0.00 -> 8.15 mm, vias 0 -> 2
- net /MCU/5V_PWM_SYNC: track 0.00 -> 7.61 mm, vias 0 -> 1
- net Net-(C89-Pad1): track 0.00 -> 6.31 mm
- net Net-(C85-Pad1): track 0.00 -> 4.65 mm
- net Net-(C83-Pad2): track 0.00 -> 3.86 mm
- net +5V_REG: track 0.00 -> 3.65 mm, vias 0 -> 5
- net /MCU/DC_IN: track 3.00 -> 6.43 mm, vias 0 -> 4
- net Net-(C91-Pad2): track 0.00 -> 3.22 mm
- net /MCU/BATT_IN: track 3.00 -> 5.52 mm
- net Net-(C92-Pad1): track 0.00 -> 1.90 mm
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- added copper zone on B.Cu, net +5V_REG
- added copper zone on B.Cu, net /MCU/BARREL_IN
- added copper zone on F.Cu, net /MCU/BARREL_IN
- added copper zone on B.Cu, net /MCU/DC_IN
- added copper zone on B.Cu, net /MCU/PERIPHERALS/SW1
- added copper zone on B.Cu, net /MCU/PERIPHERALS/SW2
- added copper zone on B.Cu, net GND
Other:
- outline, holes or cut-outs redrawn
- net class Default: clearance 0.2 -> 0.254; trace_width 0.25 -> 0.2032
- rule trace_clearance: 0.2 -> 0.254
